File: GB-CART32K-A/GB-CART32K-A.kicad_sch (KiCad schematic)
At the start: 14 parts

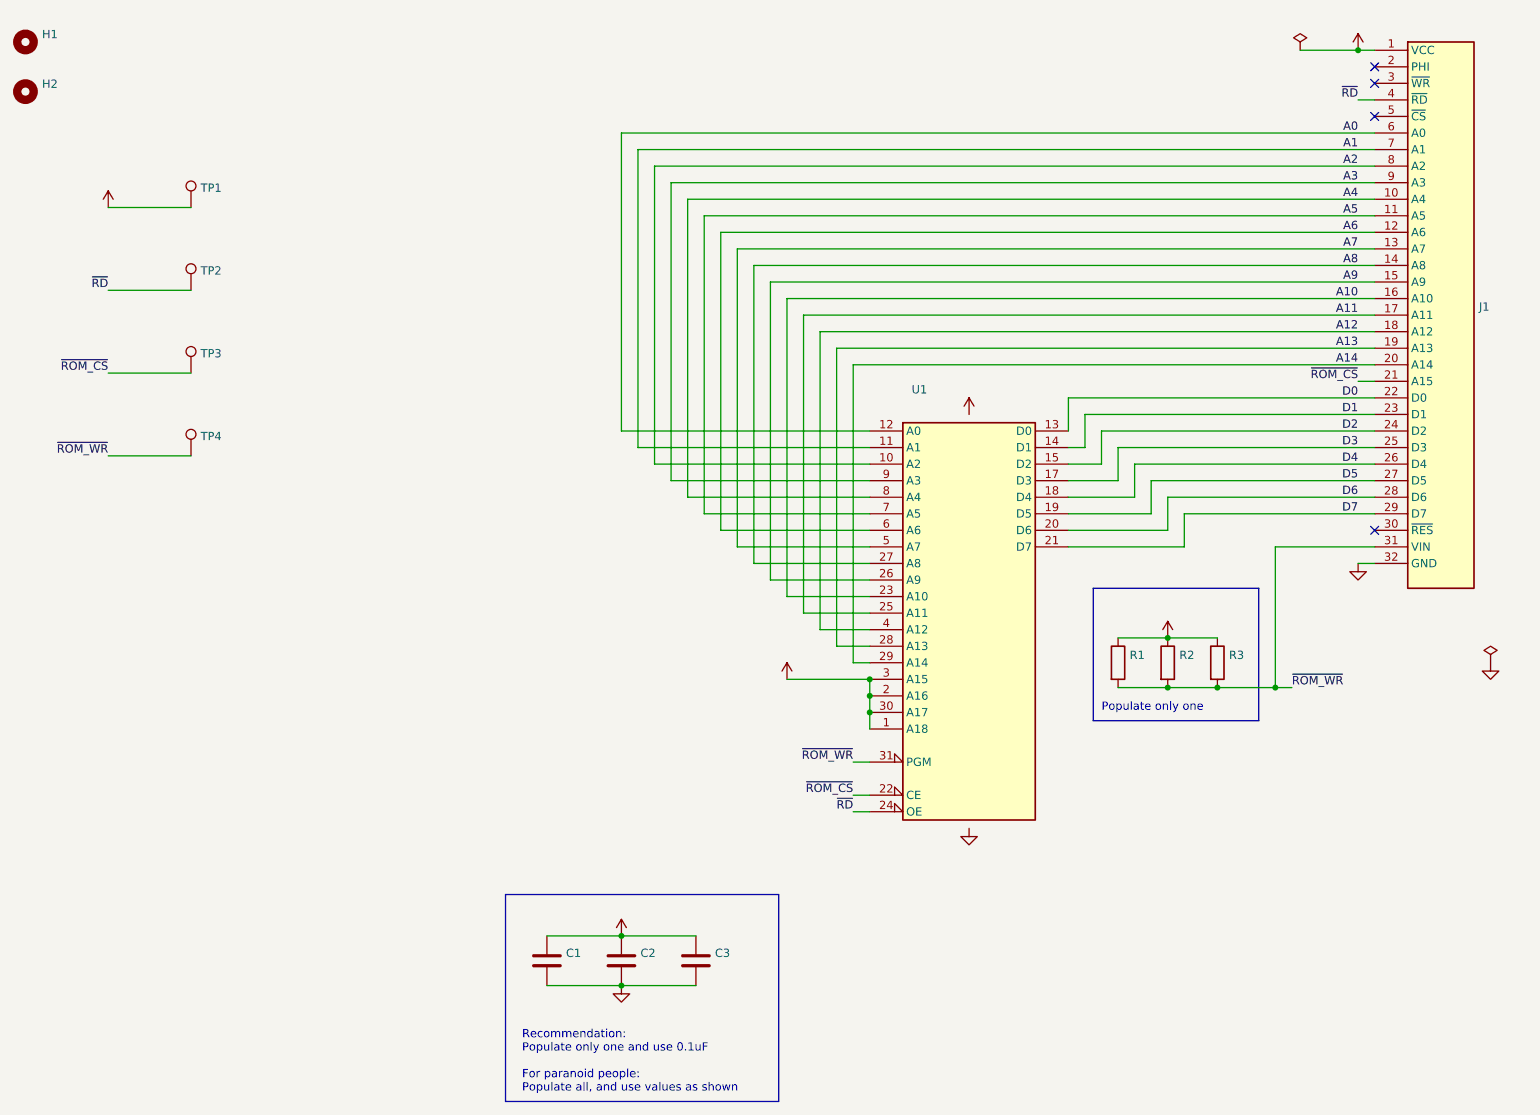
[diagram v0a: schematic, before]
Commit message: Upgrade projects to KiCad 7
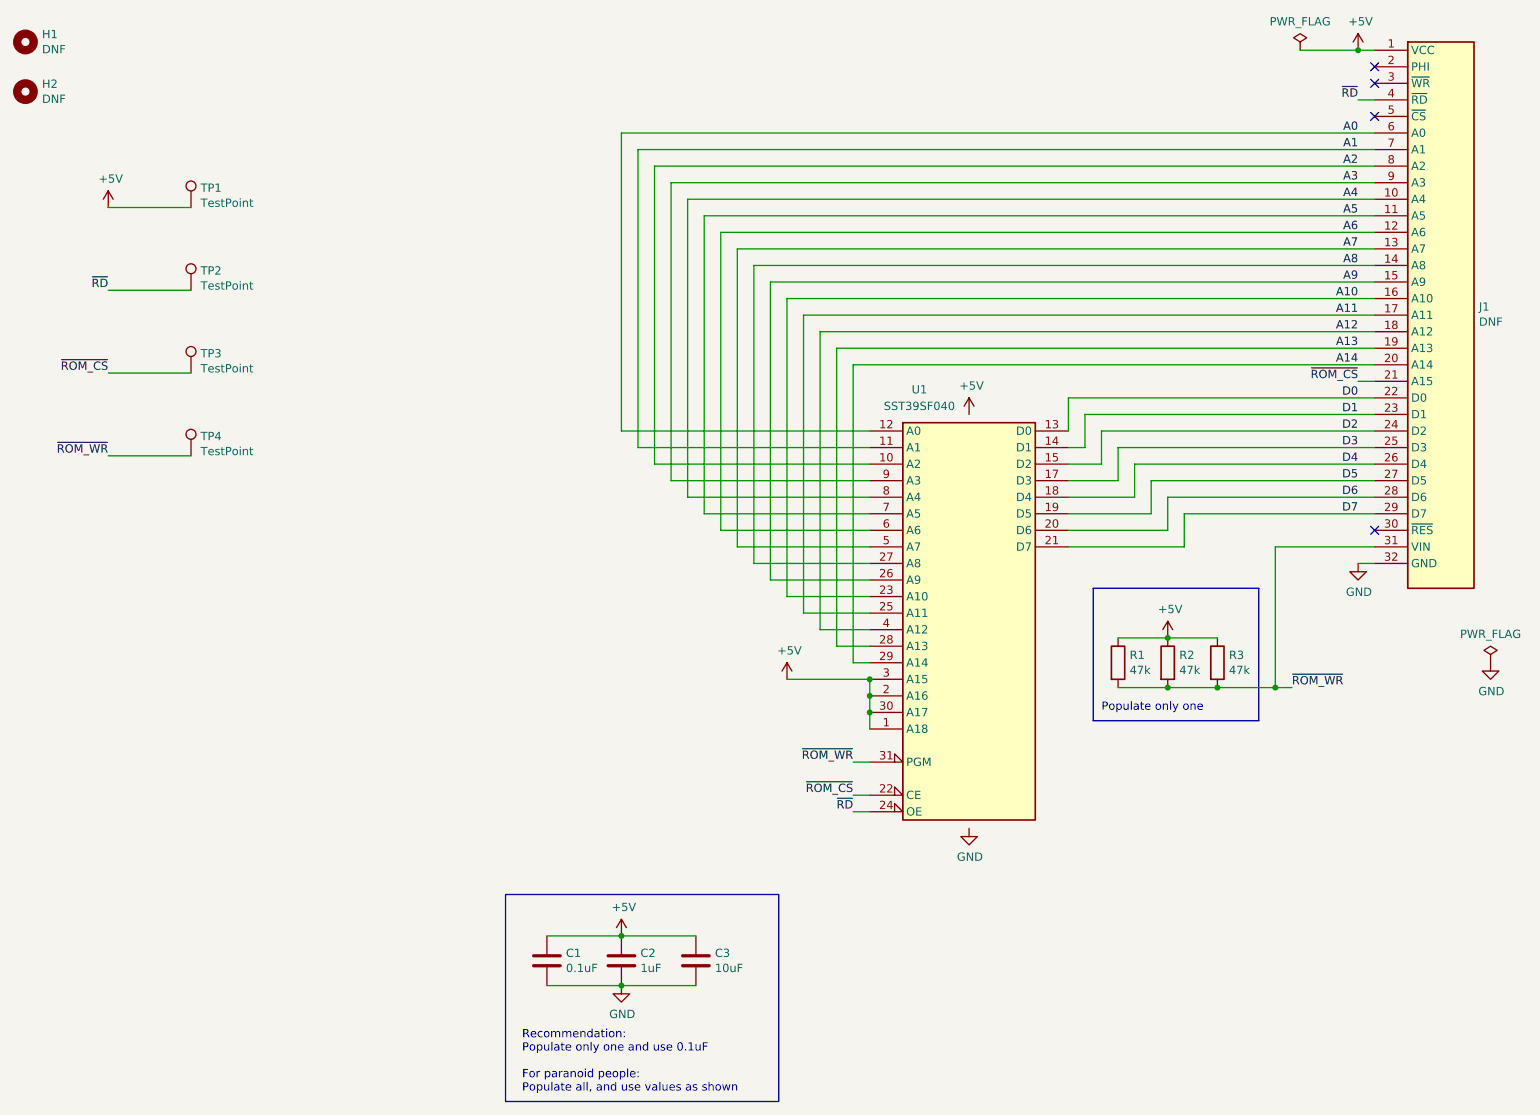
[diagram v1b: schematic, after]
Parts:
- C1: value (none) -> 0.1uF; footprint (none) -> Capacitor_SMD:C_0603_1608Metric
- C2: value (none) -> 1uF; footprint (none) -> Capacitor_SMD:C_0805_2012Metric
- C3: value (none) -> 10uF; footprint (none) -> Capacitor_SMD:C_1206_3216Metric
- H1: value (none) -> DNF; footprint (none) -> Gekkio_MountingHole:MountingHole_7.2mm
- H2: value (none) -> DNF; footprint (none) -> Gekkio_MountingHole:MountingHole_2.3mm
- J1: value (none) -> DNF; footprint (none) -> Gekkio_Connector_PCBEdge:GameBoy_Cartridge_1x32_P1.50mm_Edge
- R1: value (none) -> 47k; footprint (none) -> Resistor_SMD:R_0603_1608Metric
- R2: value (none) -> 47k; footprint (none) -> Resistor_SMD:R_0805_2012Metric
- R3: value (none) -> 47k; footprint (none) -> Resistor_SMD:R_1206_3216Metric
- TP1, TP2, TP3, TP4: value (none) -> TestPoint; footprint (none) -> TestPoint:TestPoint_THTPad_D2.0mm_Drill1.0mm
- U1: value (none) -> SST39SF040; footprint (none) -> Package_LCC:PLCC-32_11.4x14.0mm_P1.27mm
